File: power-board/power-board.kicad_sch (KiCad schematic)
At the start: 7 parts, among them J1 Conn_01x04_Female, J2 Conn_02x08_Odd_Even, J3 Conn_02x08_Odd_Even, J4 Conn_02x08_Odd_Even, J5 Conn_02x08_Odd_Even, J6 Conn_02x08_Odd_Even, J7 Conn_02x08_Odd_Even

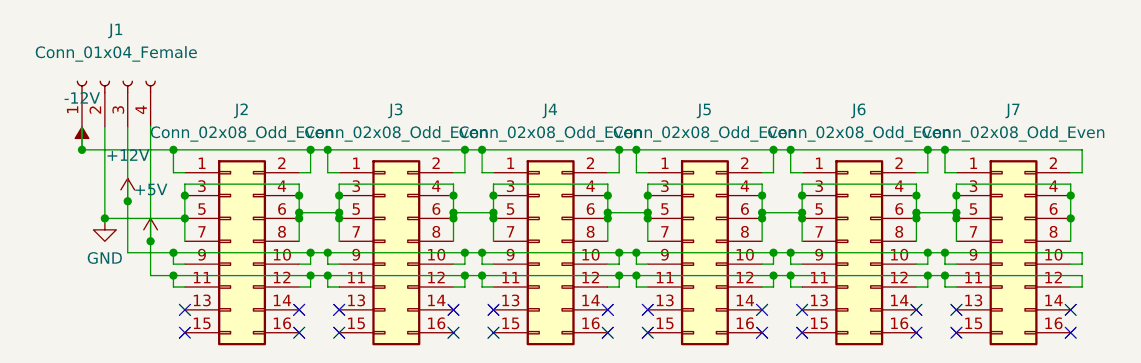
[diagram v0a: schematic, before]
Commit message: Add mounting holes to power board
And an extra trace connecting the AUX tracks (even though we're not
using them now)
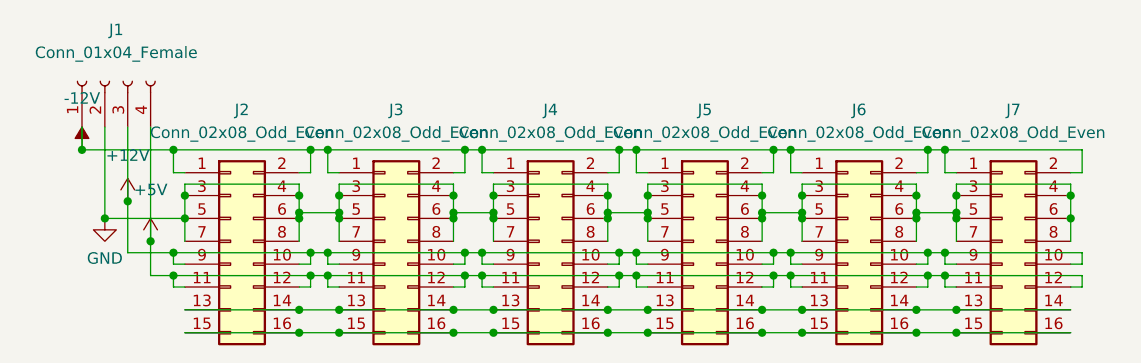
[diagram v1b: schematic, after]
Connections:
- net at J4.13 (Pin_13): now also J2.13 (Pin_13), J2.14 (Pin_14), J3.13 (Pin_13), J3.14 (Pin_14), J4.14 (Pin_14), J5.13 (Pin_13), J5.14 (Pin_14), J6.13 (Pin_13), J6.14 (Pin_14), J7.13 (Pin_13), J7.14 (Pin_14)
- net at J4.15 (Pin_15): now also J2.15 (Pin_15), J2.16 (Pin_16), J3.15 (Pin_15), J3.16 (Pin_16), J4.16 (Pin_16), J5.15 (Pin_15), J5.16 (Pin_16), J6.15 (Pin_15), J6.16 (Pin_16), J7.15 (Pin_15), J7.16 (Pin_16)
- no-connect marks 24 -> 0
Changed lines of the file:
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@@
   (junction (at 181.61 71.755) (diameter 0) (color 0 0 0 0)
   )
+  (junction (at 168.91 84.455) (diameter 0) (color 0 0 0 0)
+  )
   (junction (at 164.465 71.755) (diameter 0) (color 0 0 0 0)
   )
@@
   (junction (at 147.32 69.215) (diameter 0) (color 0 0 0 0)
   )
+  (junction (at 168.91 81.915) (diameter 0) (color 0 0 0 0)
+  )
+  (junction (at 181.61 84.455) (diameter 0) (color 0 0 0 0)
+  )
+  (junction (at 220.345 81.915) (diameter 0) (color 0 0 0 0)
+  )
   (junction (at 133.35 75.565) (diameter 0) (color 0 0 0 0)
   )
@@
   (junction (at 148.59 75.565) (diameter 0) (color 0 0 0 0)
   )
+  (junction (at 203.2 84.455) (diameter 0) (color 0 0 0 0)
+  )
   (junction (at 164.465 69.215) (diameter 0) (color 0 0 0 0)
   )
@@
   (junction (at 200.025 64.135) (diameter 0) (color 0 0 0 0)
   )
+  (junction (at 151.765 81.915) (diameter 0) (color 0 0 0 0)
+  )
   (junction (at 201.93 64.135) (diameter 0) (color 0 0 0 0)
   )
@@
   (junction (at 182.88 78.105) (diameter 0) (color 0 0 0 0)
   )
+  (junction (at 164.465 84.455) (diameter 0) (color 0 0 0 0)
+  )
+  (junction (at 186.055 81.915) (diameter 0) (color 0 0 0 0)
+  )
   (junction (at 165.735 75.565) (diameter 0) (color 0 0 0 0)
   )
@@
   (junction (at 184.785 75.565) (diameter 0) (color 0 0 0 0)
   )
+  (junction (at 164.465 81.915) (diameter 0) (color 0 0 0 0)
+  )
   (junction (at 134.62 69.215) (diameter 0) (color 0 0 0 0)
   )
   (junction (at 165.735 78.105) (diameter 0) (color 0 0 0 0)
   )
+  (junction (at 215.9 84.455) (diameter 0) (color 0 0 0 0)
+  )
   (junction (at 148.59 78.105) (diameter 0) (color 0 0 0 0)
   )
@@
   (junction (at 233.045 69.215) (diameter 0) (color 0 0 0 0)
   )
+  (junction (at 203.2 81.915) (diameter 0) (color 0 0 0 0)
+  )
+  (junction (at 215.9 81.915) (diameter 0) (color 0 0 0 0)
+  )
+  (junction (at 147.32 84.455) (diameter 0) (color 0 0 0 0)
+  )
   (junction (at 168.91 69.215) (diameter 0) (color 0 0 0 0)
   )
+  (junction (at 198.755 81.915) (diameter 0) (color 0 0 0 0)
+  )
   (junction (at 198.755 69.215) (diameter 0) (color 0 0 0 0)
   )
@@
   (junction (at 220.345 71.12) (diameter 0) (color 0 0 0 0)
   )
+  (junction (at 220.345 84.455) (diameter 0) (color 0 0 0 0)
+  )
   (junction (at 201.93 75.565) (diameter 0) (color 0 0 0 0)
   )
   (junction (at 125.73 71.755) (diameter 0) (color 0 0 0 0)
   )
+  (junction (at 198.755 84.455) (diameter 0) (color 0 0 0 0)
+  )
   (junction (at 203.2 71.755) (diameter 0) (color 0 0 0 0)
   )
@@
   (junction (at 130.81 74.295) (diameter 0) (color 0 0 0 0)
   )
+  (junction (at 151.765 84.455) (diameter 0) (color 0 0 0 0)
+  )
   (junction (at 167.64 64.135) (diameter 0) (color 0 0 0 0)
   )
   (junction (at 219.075 75.565) (diameter 0) (color 0 0 0 0)
   )
+  (junction (at 186.055 84.455) (diameter 0) (color 0 0 0 0)
+  )
+  (junction (at 147.32 81.915) (diameter 0) (color 0 0 0 0)
+  )
   (junction (at 217.17 64.135) (diameter 0) (color 0 0 0 0)
   )
@@
   (junction (at 133.35 78.105) (diameter 0) (color 0 0 0 0)
   )
-  (no_connect (at 164.465 84.455))
-  (no_connect (at 220.345 81.915))
-  (no_connect (at 164.465 81.915))
-  (no_connect (at 168.91 81.915))
-  (no_connect (at 233.045 81.915))
-  (no_connect (at 198.755 84.455))
-  (no_connect (at 168.91 84.455))
-  (no_connect (at 186.055 84.455))
-  (no_connect (at 203.2 84.455))
-  (no_connect (at 181.61 81.915))
-  (no_connect (at 186.055 81.915))
-  (no_connect (at 215.9 81.915))
-  (no_connect (at 215.9 84.455))
-  (no_connect (at 203.2 81.915))
-  (no_connect (at 151.765 81.915))
-  (no_connect (at 233.045 84.455))
-  (no_connect (at 151.765 84.455))
-  (no_connect (at 147.32 81.915))
-  (no_connect (at 147.32 84.455))
-  (no_connect (at 134.62 81.915))
-  (no_connect (at 134.62 84.455))
-  (no_connect (at 198.755 81.915))
-  (no_connect (at 181.61 84.455))
-  (no_connect (at 220.345 84.455))
+  (junction (at 181.61 81.915) (diameter 0) (color 0 0 0 0)
+  )
   (wire (pts (xy 150.495 76.835) (xy 150.495 75.565))
     (stroke (width 0) (type default) (color 0 0 0 0))
@@
     (stroke (width 0) (type default) (color 0 0 0 0))
   )
+  (wire (pts (xy 181.61 81.915) (xy 186.055 81.915))
+    (stroke (width 0) (type default) (color 0 0 0 0))
+  )
   (wire (pts (xy 164.465 71.12) (xy 164.465 71.755))
     (stroke (width 0) (type default) (color 0 0 0 0))
@@
     (stroke (width 0) (type default) (color 0 0 0 0))
   )
+  (wire (pts (xy 134.62 84.455) (xy 147.32 84.455))
+    (stroke (width 0) (type default) (color 0 0 0 0))
+  )
   (wire (pts (xy 168.91 67.945) (xy 181.61 67.945))
     (stroke (width 0) (type default) (color 0 0 0 0))
@@
     (stroke (width 0) (type default) (color 0 0 0 0))
   )
+  (wire (pts (xy 186.055 84.455) (xy 198.755 84.455))
+    (stroke (width 0) (type default) (color 0 0 0 0))
+  )
   (wire (pts (xy 186.055 79.375) (xy 184.785 79.375))
     (stroke (width 0) (type default) (color 0 0 0 0))
@@
     (stroke (width 0) (type default) (color 0 0 0 0))
   )
+  (wire (pts (xy 181.61 84.455) (xy 186.055 84.455))
+    (stroke (width 0) (type default) (color 0 0 0 0))
+  )
   (wire (pts (xy 147.32 71.12) (xy 151.765 71.12))
     (stroke (width 0) (type default) (color 0 0 0 0))
@@
     (stroke (width 0) (type default) (color 0 0 0 0))
   )
+  (wire (pts (xy 198.755 81.915) (xy 203.2 81.915))
+    (stroke (width 0) (type default) (color 0 0 0 0))
+  )
   (wire (pts (xy 234.315 78.105) (xy 234.315 79.375))
     (stroke (width 0) (type default) (color 0 0 0 0))
@@
     (stroke (width 0) (type default) (color 0 0 0 0))
   )
+  (wire (pts (xy 198.755 84.455) (xy 203.2 84.455))
+    (stroke (width 0) (type default) (color 0 0 0 0))
+  )
   (wire (pts (xy 167.64 78.105) (xy 182.88 78.105))
     (stroke (width 0) (type default) (color 0 0 0 0))
@@
     (stroke (width 0) (type default) (color 0 0 0 0))
   )
+  (wire (pts (xy 134.62 81.915) (xy 147.32 81.915))
+    (stroke (width 0) (type default) (color 0 0 0 0))
+  )
   (wire (pts (xy 181.61 69.215) (xy 181.61 71.12))
     (stroke (width 0) (type default) (color 0 0 0 0))
@@
     (stroke (width 0) (type default) (color 0 0 0 0))
   )
+  (wire (pts (xy 164.465 84.455) (xy 168.91 84.455))
+    (stroke (width 0) (type default) (color 0 0 0 0))
+  )
   (wire (pts (xy 203.2 67.945) (xy 215.9 67.945))
     (stroke (width 0) (type default) (color 0 0 0 0))
@@
     (stroke (width 0) (type default) (color 0 0 0 0))
   )
+  (wire (pts (xy 164.465 81.915) (xy 168.91 81.915))
+    (stroke (width 0) (type default) (color 0 0 0 0))
+  )
   (wire (pts (xy 182.88 75.565) (xy 184.785 75.565))
     (stroke (width 0) (type default) (color 0 0 0 0))
   )
+  (wire (pts (xy 168.91 81.915) (xy 181.61 81.915))
+    (stroke (width 0) (type default) (color 0 0 0 0))
+  )
   (wire (pts (xy 133.35 64.135) (xy 123.19 64.135))
     (stroke (width 0) (type default) (color 0 0 0 0))
@@
     (stroke (width 0) (type default) (color 0 0 0 0))
   )
+  (wire (pts (xy 203.2 84.455) (xy 215.9 84.455))
+    (stroke (width 0) (type default) (color 0 0 0 0))
+  )
   (wire (pts (xy 147.32 71.12) (xy 147.32 71.755))
     (stroke (width 0) (type default) (color 0 0 0 0))
@@
     (stroke (width 0) (type default) (color 0 0 0 0))
   )
+  (wire (pts (xy 151.765 81.915) (xy 164.465 81.915))
+    (stroke (width 0) (type default) (color 0 0 0 0))
+  )
   (wire (pts (xy 186.055 71.755) (xy 186.055 74.295))
     (stroke (width 0) (type default) (color 0 0 0 0))
   )
+  (wire (pts (xy 215.9 81.915) (xy 220.345 81.915))
+    (stroke (width 0) (type default) (color 0 0 0 0))
+  )
   (wire (pts (xy 133.35 79.375) (xy 133.35 78.105))
     (stroke (width 0) (type default) (color 0 0 0 0))
   )
+  (wire (pts (xy 147.32 81.915) (xy 151.765 81.915))
+    (stroke (width 0) (type default) (color 0 0 0 0))
+  )
   (wire (pts (xy 220.345 76.835) (xy 219.075 76.835))
     (stroke (width 0) (type default) (color 0 0 0 0))
@@
     (stroke (width 0) (type default) (color 0 0 0 0))
   )
+  (wire (pts (xy 220.345 81.915) (xy 233.045 81.915))
+    (stroke (width 0) (type default) (color 0 0 0 0))
+  )
   (wire (pts (xy 181.61 67.945) (xy 181.61 69.215))
     (stroke (width 0) (type default) (color 0 0 0 0))
@@
     (stroke (width 0) (type default) (color 0 0 0 0))
   )
+  (wire (pts (xy 215.9 84.455) (xy 220.345 84.455))
+    (stroke (width 0) (type default) (color 0 0 0 0))
+  )
   (wire (pts (xy 233.045 79.375) (xy 234.315 79.375))
     (stroke (width 0) (type default) (color 0 0 0 0))
@@
     (stroke (width 0) (type default) (color 0 0 0 0))
   )
+  (wire (pts (xy 220.345 84.455) (xy 233.045 84.455))
+    (stroke (width 0) (type default) (color 0 0 0 0))
+  )
   (wire (pts (xy 151.765 79.375) (xy 150.495 79.375))
     (stroke (width 0) (type default) (color 0 0 0 0))
@@
     (stroke (width 0) (type default) (color 0 0 0 0))
   )
+  (wire (pts (xy 168.91 84.455) (xy 181.61 84.455))
+    (stroke (width 0) (type default) (color 0 0 0 0))
+  )
   (wire (pts (xy 198.755 71.755) (xy 198.755 74.295))
     (stroke (width 0) (type default) (color 0 0 0 0))
@@
     (stroke (width 0) (type default) (color 0 0 0 0))
   )
+  (wire (pts (xy 147.32 84.455) (xy 151.765 84.455))
+    (stroke (width 0) (type default) (color 0 0 0 0))
+  )
   (wire (pts (xy 219.075 79.375) (xy 219.075 78.105))
     (stroke (width 0) (type default) (color 0 0 0 0))
@@
     (stroke (width 0) (type default) (color 0 0 0 0))
   )
+  (wire (pts (xy 186.055 81.915) (xy 198.755 81.915))
+    (stroke (width 0) (type default) (color 0 0 0 0))
+  )
   (wire (pts (xy 130.81 61.595) (xy 130.81 74.295))
     (stroke (width 0) (type default) (color 0 0 0 0))
   )
+  (wire (pts (xy 151.765 84.455) (xy 164.465 84.455))
+    (stroke (width 0) (type default) (color 0 0 0 0))
+  )
   (wire (pts (xy 182.88 64.135) (xy 182.88 66.675))
     (stroke (width 0) (type default) (color 0 0 0 0))
@@
     (stroke (width 0) (type default) (color 0 0 0 0))
   )
+  (wire (pts (xy 203.2 81.915) (xy 215.9 81.915))
+    (stroke (width 0) (type default) (color 0 0 0 0))
+  )
